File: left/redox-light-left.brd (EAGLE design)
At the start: 161 x 125.5 mm, 136 parts, among them IC36 STM32F103TXUX, X1 USBMICRO_B, X2 AUDIO-JACKSMD

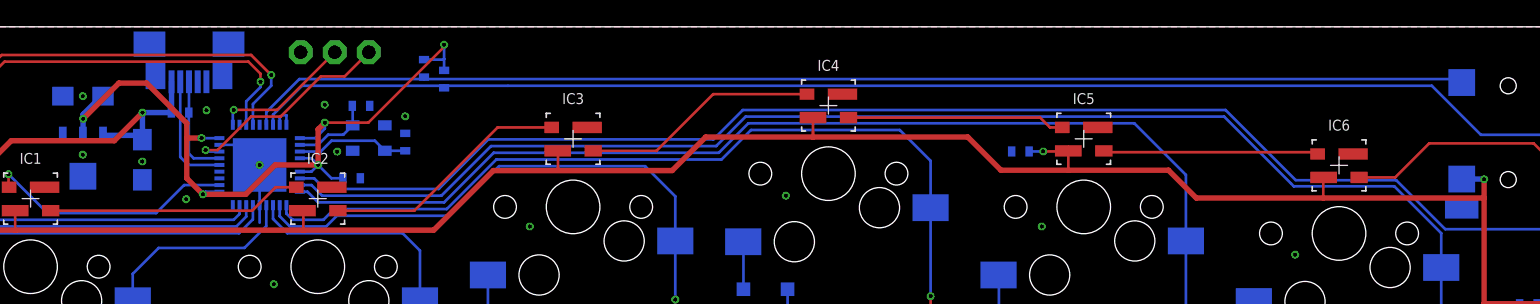
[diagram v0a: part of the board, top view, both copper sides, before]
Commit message: replace swd connector with tps, move files
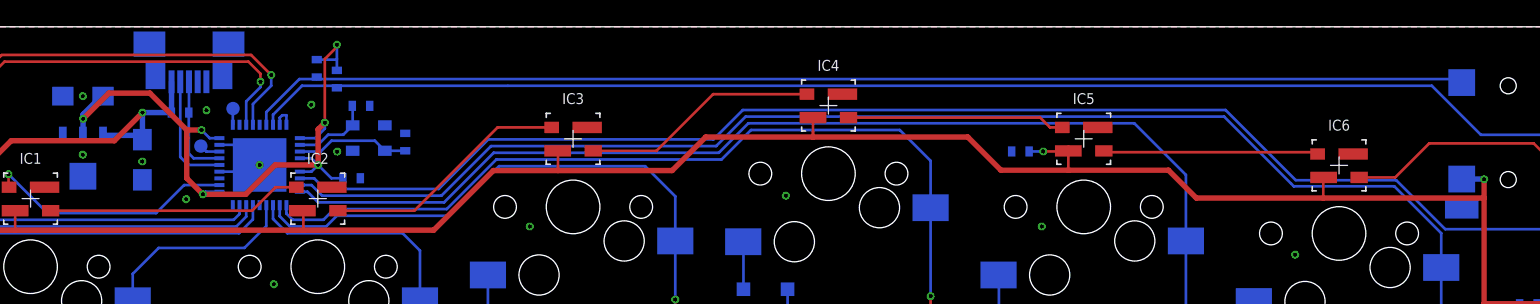
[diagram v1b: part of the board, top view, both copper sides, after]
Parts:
- removed X3: (no value), netcat:1X03
- added TP1: CLK, netcat:TP10R
- added TP2: IO, netcat:TP10R
- moved R2 8.00 mm to (28.5, 116.4)
- moved R3 8.00 mm to (30.0, 115.6)
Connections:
- net GND: now also IC36.22; no longer IC36.14, X3.1
- net SWD_CLK: now also TP1.TP; no longer X3.2
- net SWD_IO: now also TP2.TP; no longer X3.3
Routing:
- net SWD_IO: track 16.3 -> 1.55 mm, vias 1 -> 0
- net SWD_CLK: track 10.5 -> 1.22 mm, vias 1 -> 0
- net VCC: track 58.9 -> 53.0 mm
- net GND: track 12.7 -> 11.9 mm, vias 46 -> 45

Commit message: some improoves
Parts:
- added R4: 4.7k, netcat:R0402
- moved C22 1.06 mm to (31.8, 107.4)
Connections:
- new net N$35: IC36.4, R4.1
- net VCC: now also R4.2; no longer IC36.4
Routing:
- net VCC: track 53.0 -> 59.0 mm, vias 6 -> 7
- net N$35: track 0.00 -> 4.37 mm
- net COL5: track 186.1 -> 186.7 mm
- net COL4: track 158.9 -> 159.6 mm
- net COL6: track 221.1 -> 221.8 mm

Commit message: lm1117 pkg fix
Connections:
- net GND: no longer IC37.4
- net VCC: now also IC37.4
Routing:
- net VCC: track 59.0 -> 62.1 mm
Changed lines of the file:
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@@
 <wire x1="33.7" y1="108.6" x2="33.309" y2="108.991" width="0.2" layer="1"/>
 <wire x1="33.309" y1="108.991" x2="28.6" y2="108.991" width="0.2" layer="1"/>
+<contactref element="IC37" pad="4"/>
+<wire x1="11.05" y1="111.45" x2="11.05" y2="108.35" width="0.4064" layer="16"/>
 </signal>
 <signal name="GND">
@@
 <contactref element="X1" pad="6"/>
 <contactref element="X1" pad="GND"/>
-<contactref element="IC37" pad="4"/>
 <contactref element="C1" pad="-"/>
 <contactref element="C3" pad="2"/>
@@
 <wire x1="25.92" y1="112.9" x2="25.735" y2="112.715" width="0.2" layer="16"/>
 <via x="18.75" y="106.64" extent="1-16" drill="0.3"/>
-<via x="11.04" y="109.96" extent="1-16" drill="0.3"/>
+<via x="9.54" y="110.06" extent="1-16" drill="0.3"/>
 <via x="15.48" y="109.45" extent="1-16" drill="0.3"/>
 <via x="11.05" y="114.33" extent="1-16" drill="0.3"/>
